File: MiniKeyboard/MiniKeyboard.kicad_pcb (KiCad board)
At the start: 2 copper layers, 135.9 x 106.7 mm, 102 parts, among them J1 Conn_01x04_Female, J2 Conn_01x04_Female, J3 Conn_01x03_Male, SW1 SW_Push, SW10 SW_Push, SW11 SW_Push, SW12 SW_Push, SW13 SW_Push, SW14 SW_Push, SW15 SW_Push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

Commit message: mini keyboard progress
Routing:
- added copper zone on F.Cu, net +5V
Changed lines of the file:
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@@
   (gr_line (start 112.141 134.747) (end 112.141 139.827) (layer B.SilkS) (width 0.12))
   (gr_line (start 97.79 134.747) (end 112.141 134.747) (layer B.SilkS) (width 0.12))
-  (gr_line (start 112.522 57.531) (end 119.761 57.531) (layer B.SilkS) (width 0.12))
-  (gr_line (start 112.522 64.262) (end 119.761 64.262) (layer B.SilkS) (width 0.12))
-  (gr_line (start 129.54 57.531) (end 121.158 57.531) (layer B.SilkS) (width 0.12))
-  (gr_line (start 101.981 64.262) (end 111.125 64.262) (layer B.SilkS) (width 0.12))
-  (gr_line (start 111.125 57.531) (end 101.981 57.531) (layer B.SilkS) (width 0.12))
+  (gr_line (start 112.522 48.006) (end 119.761 48.006) (layer B.SilkS) (width 0.12))
+  (gr_line (start 112.522 54.737) (end 119.761 54.737) (layer B.SilkS) (width 0.12))
+  (gr_line (start 129.54 48.006) (end 121.158 48.006) (layer B.SilkS) (width 0.12))
+  (gr_line (start 101.981 54.737) (end 111.125 54.737) (layer B.SilkS) (width 0.12))
+  (gr_line (start 111.125 48.006) (end 101.981 48.006) (layer B.SilkS) (width 0.12))
   (gr_line (start 116.459 144.78) (end 123.825 144.78) (layer B.SilkS) (width 0.12))
   (gr_line (start 120.015 144.78) (end 120.015 148.336) (layer B.SilkS) (width 0.12))
@@
   (gr_line (start 116.459 148.463) (end 123.825 148.463) (layer B.SilkS) (width 0.12))
   (gr_line (start 116.459 144.78) (end 116.459 148.463) (layer B.SilkS) (width 0.12))
-  (gr_line (start 124.968 57.531) (end 124.968 59.436) (layer B.SilkS) (width 0.12))
-  (gr_line (start 121.158 57.531) (end 121.158 59.436) (layer B.SilkS) (width 0.12))
-  (gr_line (start 129.54 59.436) (end 121.158 59.436) (layer B.SilkS) (width 0.12))
-  (gr_line (start 129.54 57.531) (end 129.54 59.436) (layer B.SilkS) (width 0.12))
-  (gr_line (start 115.824 57.531) (end 115.824 64.262) (layer B.SilkS) (width 0.12))
-  (gr_line (start 112.522 64.262) (end 112.522 57.531) (layer B.SilkS) (width 0.12))
-  (gr_line (start 111.125 57.531) (end 111.125 64.262) (layer B.SilkS) (width 0.12))
-  (gr_line (start 106.68 57.531) (end 106.68 64.262) (layer B.SilkS) (width 0.12))
-  (gr_line (start 101.981 62.611) (end 101.981 60.833) (layer B.SilkS) (width 0.12))
-  (gr_line (start 101.981 64.262) (end 101.981 57.531) (layer B.SilkS) (width 0.12))
-  (gr_line (start 119.761 57.531) (end 119.761 64.262) (layer B.SilkS) (width 0.12))
+  (gr_line (start 124.968 48.006) (end 124.968 49.911) (layer B.SilkS) (width 0.12))
+  (gr_line (start 121.158 48.006) (end 121.158 49.911) (layer B.SilkS) (width 0.12))
+  (gr_line (start 129.54 49.911) (end 121.158 49.911) (layer B.SilkS) (width 0.12))
+  (gr_line (start 129.54 48.006) (end 129.54 49.911) (layer B.SilkS) (width 0.12))
+  (gr_line (start 115.824 48.006) (end 115.824 54.737) (layer B.SilkS) (width 0.12))
+  (gr_line (start 112.522 54.737) (end 112.522 48.006) (layer B.SilkS) (width 0.12))
+  (gr_line (start 111.125 48.006) (end 111.125 54.737) (layer B.SilkS) (width 0.12))
+  (gr_line (start 106.68 48.006) (end 106.68 54.737) (layer B.SilkS) (width 0.12))
+  (gr_line (start 101.981 53.086) (end 101.981 51.308) (layer B.SilkS) (width 0.12))
+  (gr_line (start 101.981 54.737) (end 101.981 48.006) (layer B.SilkS) (width 0.12))
+  (gr_line (start 119.761 48.006) (end 119.761 54.737) (layer B.SilkS) (width 0.12))
   (gr_text "F411C\nPA15\nPB3" (at 102.743 137.287) (layer B.SilkS)
     (effects (font (size 1 1) (thickness 0.15)) (justify left mirror))
@@
     (effects (font (size 1 1) (thickness 0.15)) (justify left mirror))
   )
-  (gr_text PA7 (at 122.936 58.42) (layer B.SilkS)
+  (gr_text PA7 (at 122.936 48.895) (layer B.SilkS)
     (effects (font (size 1 1) (thickness 0.15)) (justify mirror))
   )
-  (gr_text LEDs (at 127.254 58.42) (layer B.SilkS)
+  (gr_text LEDs (at 127.254 48.895) (layer B.SilkS)
     (effects (font (size 1 1) (thickness 0.15)) (justify mirror))
   )
@@
     (effects (font (size 1 1) (thickness 0.15)) (justify mirror))
   )
-  (gr_text "PB12\nPB13\nPB14\nPB15" (at 104.521 60.96) (layer B.SilkS)
+  (gr_text "PB12\nPB13\nPB14\nPB15" (at 104.521 51.435) (layer B.SilkS)
     (effects (font (size 1 1) (thickness 0.15)) (justify mirror))
   )
-  (gr_text "PA0\nPA1\nPA2\nPA3" (at 114.046 60.96) (layer B.SilkS)
+  (gr_text "PA0\nPA1\nPA2\nPA3" (at 114.046 51.435) (layer B.SilkS)
     (effects (font (size 1 1) (thickness 0.15)) (justify mirror))
   )
-  (gr_text "Row0\nRow1\nRow2\nRow3" (at 108.966 60.96) (layer B.SilkS)
+  (gr_text "Row0\nRow1\nRow2\nRow3" (at 108.966 51.435) (layer B.SilkS)
     (effects (font (size 1 1) (thickness 0.15)) (justify mirror))
   )
-  (gr_text "Col0\nCol1\nCol2\nCol3" (at 117.856 60.96) (layer B.SilkS)
+  (gr_text "Col0\nCol1\nCol2\nCol3" (at 117.856 51.435) (layer B.SilkS)
     (effects (font (size 1 1) (thickness 0.15)) (justify mirror))
   )
@@
       )
     )
+  )
+  (zone (net 2) (net_name +5V) (layer F.Cu) (hatch edge 0.508)
+    (connect_pads (clearance 0.508))
+    (min_thickness 0.254)
+    (fill yes (arc_segments 32) (thermal_gap 0.508) (thermal_bridge_width 0.508))
+    (polygon
+      (pts
+        (xy 226.06 59.69) (xy 222.885 59.69) (xy 222.885 64.77) (xy 226.06 64.77) (xy 226.06 152.4)
+        (xy 90.17 152.4) (xy 90.17 125.73) (xy 93.345 125.73) (xy 93.345 120.65) (xy 90.17 120.65)
+        (xy 90.17 64.77) (xy 93.98 64.77) (xy 93.98 59.69) (xy 90.17 59.69) (xy 90.17 45.72)
+        (xy 226.06 45.72)
+      )
+    )

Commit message: moved user info text to using kibuzzard generated labels
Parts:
- added svg2mod: G***, label, F.Cu at (220.2, 125.0)
- added svg2mod: G***, label, F.Cu at (111.8, 142.0)
- added svg2mod: G***, label, F.Cu at (109.2, 142.0)
- added svg2mod: G***, label, F.Cu at (106.7, 142.0)
- added svg2mod: G***, label, F.Cu at (99.8, 136.7)
- added svg2mod: G***, label, F.Cu at (99.8, 128.8)
- added svg2mod: G***, label, F.Cu at (99.8, 134.1)
- added svg2mod: G***, label, F.Cu at (99.8, 131.3)
- added svg2mod: G***, label, F.Cu at (168.4, 55.8)
- added svg2mod: G***, label, F.Cu at (189.0, 55.8)
- added svg2mod: G***, label, F.Cu at (148.6, 56.0)
- added svg2mod: G***, label, F.Cu at (220.0, 127.5)
- added svg2mod: G***, label, F.Cu at (220.0, 98.0)
- added svg2mod: G***, label, F.Cu at (220.5, 122.4)
- added svg2mod: G***, label, F.Cu at (215.9, 125.2)
- added svg2mod: G***, label, F.Cu at (111.3, 123.7)
- added svg2mod: G***, label, F.Cu at (103.9, 68.6)
- added svg2mod: G***, label, F.Cu at (110.5, 148.6)
- added svg2mod: G***, label, F.Cu at (93.0, 132.6)
- added svg2mod: G***, label, F.Cu at (114.3, 142.0)
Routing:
- net /RX: track 61.9 -> 67.6 mm
- net GND: track 856.5 -> 861.5 mm
- net /TX: track 60.1 -> 64.3 mm
- net +5V: track 926.1 -> 925.6 mm, vias 29 -> 33
- net Net-(D3-Pad2): vias 2 -> 0
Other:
- board text removed: "3.3V"
- board text removed: "5V"
- board text removed: "Caps"
- board text removed: "DO"
- board text removed: "Debug UART"
- board text removed: "F103C8 Bluepill"
- board text removed: "F411CE Blackpill"
- board text removed: "GND"
- board text removed: "Num"
- board text removed: "OLED"
- board text removed: "RX"
- board text removed: "SCL"
- board text removed: "SDA"
- board text removed: "Scroll"
- board text removed: "TX"

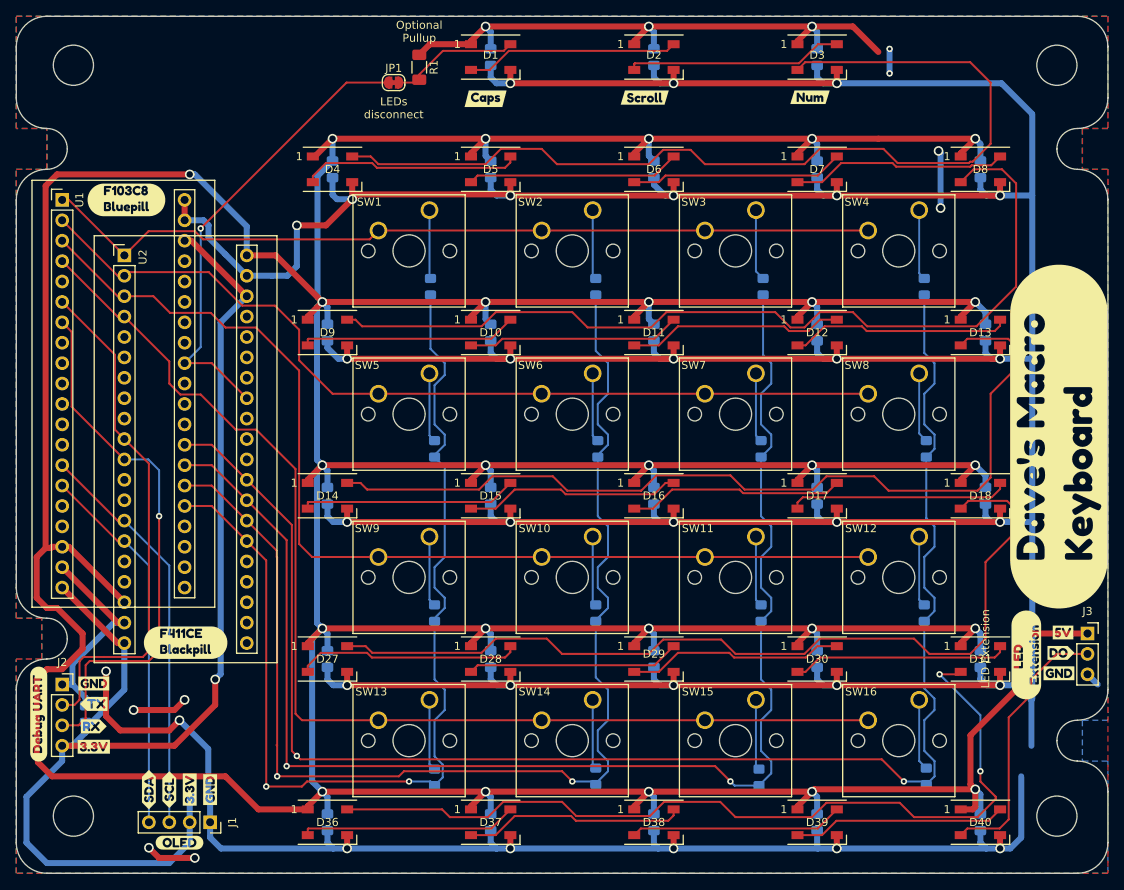
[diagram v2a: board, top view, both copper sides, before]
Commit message: changed minikeyboard diodes and generated gerbers
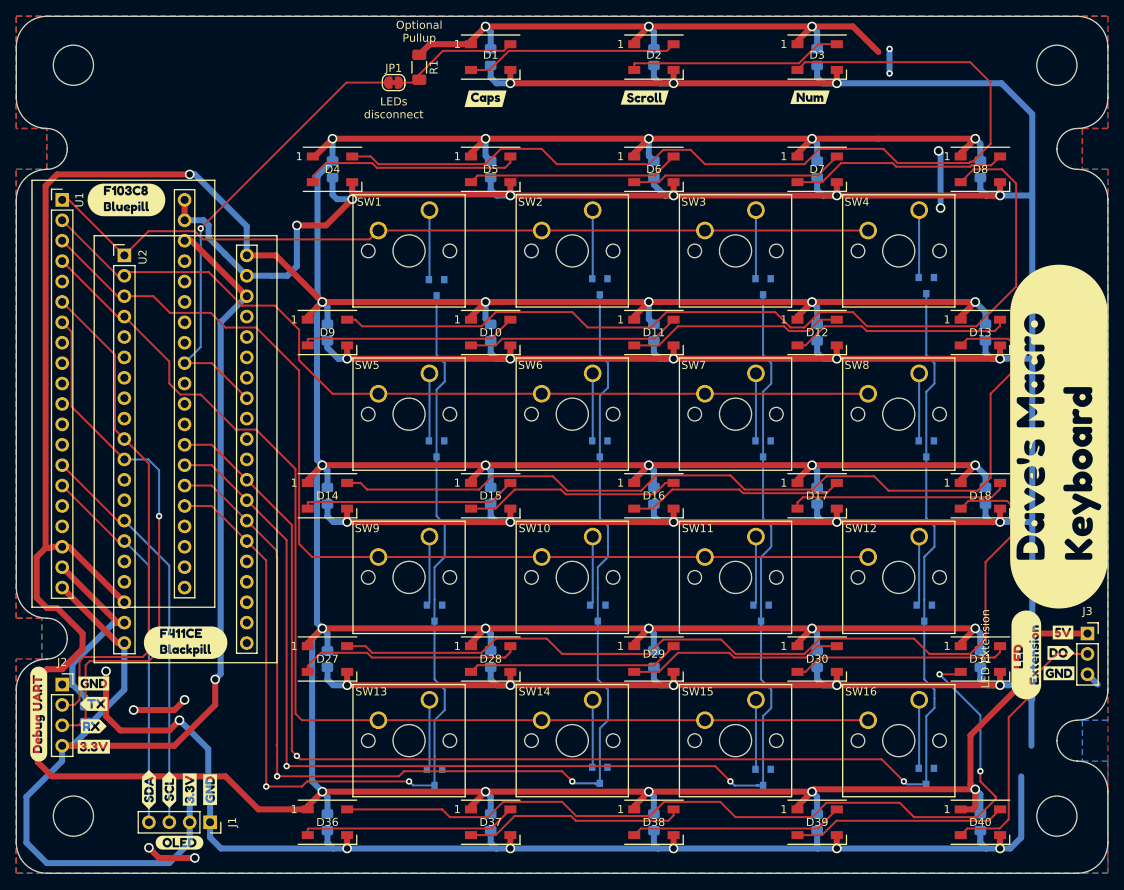
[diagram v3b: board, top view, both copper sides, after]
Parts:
- D19, D20, D21, D22, D23, D24, D25, D26, D32, D33, D34, D35, D41, D42, D43, D44: footprint Diode_SMD:D_0805_2012Metric_Pad1.15x1.40mm_HandSolder -> Diode_SMD:D_SOT-23_ANK
- moved D19 0.77 mm to (142.5, 79.5), turned to 270 degrees
- moved D42 0.52 mm to (162.8, 140.2), turned to 270 degrees
- moved D20 0.51 mm to (162.8, 79.4), turned to 270 degrees
- moved D43 0.51 mm to (183.1, 140.5), turned to 270 degrees
- moved D22 0.29 mm to (203.5, 79.2), turned to 270 degrees
- moved D23 0.25 mm to (142.5, 99.6), turned to 270 degrees
- moved D24 0.25 mm to (162.8, 99.6), turned to 270 degrees
- moved D25 0.25 mm to (183.1, 99.6), turned to 270 degrees
- moved D33 0.25 mm to (162.6, 120.0), turned to 270 degrees
- turned D21 to 270 degrees
- turned D26 to 270 degrees
- turned D32 to 270 degrees
- turned D34 to 270 degrees
- turned D35 to 270 degrees
- turned D41 to 270 degrees
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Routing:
- net /Col1: track 151.4 -> 148.0 mm
- net /Col0: track 129.9 -> 127.0 mm
- net /Col2: track 171.9 -> 169.1 mm
- net /Col3: track 193.3 -> 190.7 mm
